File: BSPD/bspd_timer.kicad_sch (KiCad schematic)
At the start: 6 parts, among them U20 HEF4093B, U21 LM555N

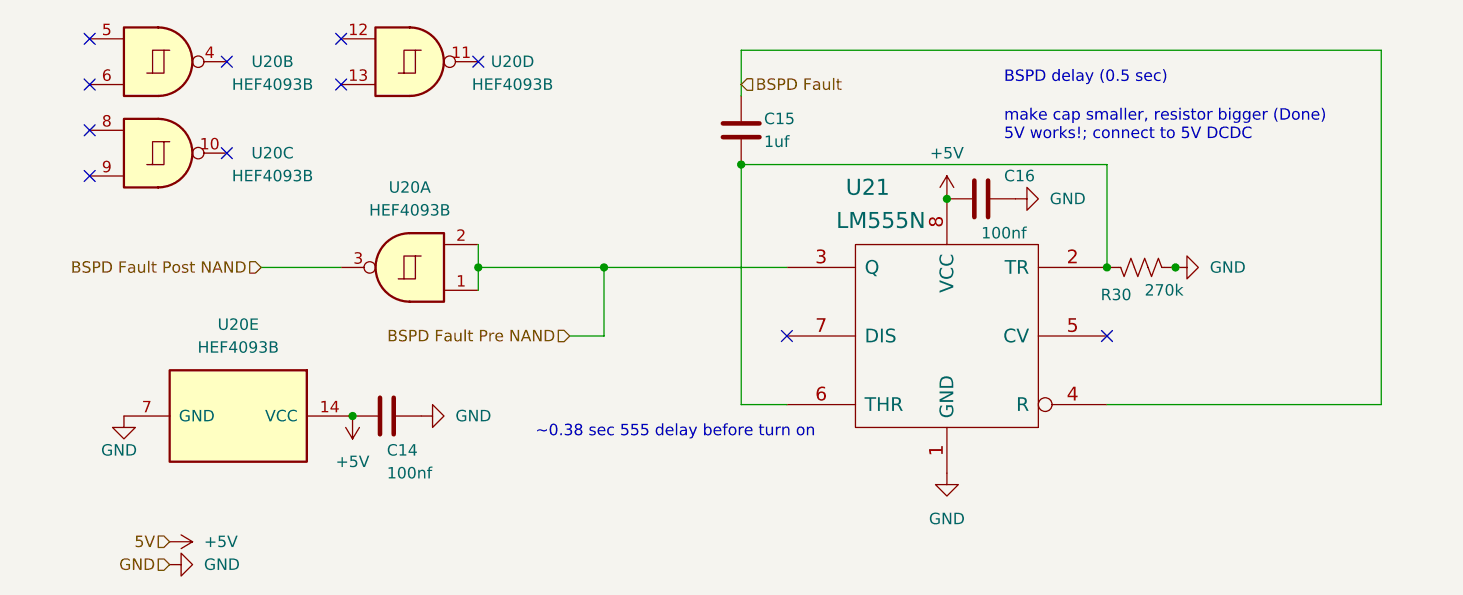
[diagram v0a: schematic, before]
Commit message: Overhaul of BPSD to V3.0
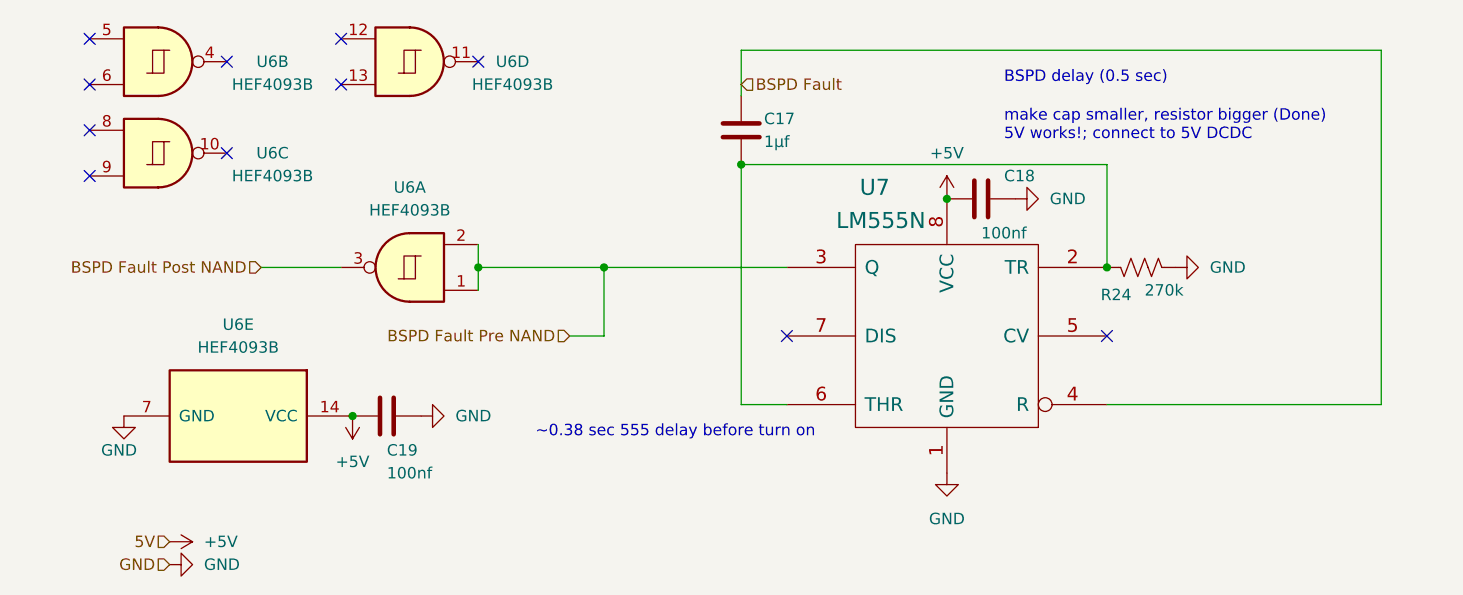
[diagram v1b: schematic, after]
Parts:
- C17: renamed from C15; value 1uf -> 1μf
- renumbered C16 to C18, C14 to C19, R30 to R24, U20 to U6, U21 to U7
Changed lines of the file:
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@@
-	)
-	(junction
-		(at 139.7 44.45)
-		(diameter 0)
-		(color 0 0 0 0)
 	)
 	(junction
@@
 		(pts
 			(xy 46.99 44.45) (xy 38.1 44.45)
-		)
-		(stroke
-			(width 0)
-			(type default)
-		)
-	)
-	(wire
-		(pts
-			(xy 139.7 44.45) (xy 139.7 44.323)
 		)
 		(stroke
@@
 		(on_board yes)
 		(dnp no)
-		(property "Reference" "C14"
+		(property "Reference" "C19"
 			(at 52.07 64.77 90)
 			(effects
@@
 			(project "BSPD"
 				(path "/9b958334-fa88-4811-8197-71444a07b1b5/5dba9582-9d62-469b-9332-e1b404bf542e"
-					(reference "C14")
+					(reference "C19")
 					(unit 1)
 				)
@@
 		(on_board yes)
 		(dnp no)
-		(property "Reference" "R30"
+		(property "Reference" "R24"
 			(at 133.096 47.498 90)
 			(effects
@@
 			(project "BSPD"
 				(path "/9b958334-fa88-4811-8197-71444a07b1b5/5dba9582-9d62-469b-9332-e1b404bf542e"
-					(reference "R30")
+					(reference "R24")
 					(unit 1)
 				)
@@
 		(dnp no)
 		(fields_autoplaced yes)
-		(property "Reference" "U20"
+		(property "Reference" "U6"
 			(at 35.56 50.8 90)
 			(effects
@@
 			(project "BSPD"
 				(path "/9b958334-fa88-4811-8197-71444a07b1b5/5dba9582-9d62-469b-9332-e1b404bf542e"
-					(reference "U20")
+					(reference "U6")
 					(unit 5)
 				)
@@
 		(on_board yes)
 		(dnp no)
-		(property "Reference" "U20"
+		(property "Reference" "U6"
 			(at 66.04 21.59 0)
 			(effects
@@
 			(project "BSPD"
 				(path "/9b958334-fa88-4811-8197-71444a07b1b5/5dba9582-9d62-469b-9332-e1b404bf542e"
-					(reference "U20")
+					(reference "U6")
 					(unit 4)
 				)
@@
 		(dnp no)
 		(fields_autoplaced yes)
-		(property "Reference" "U20"
+		(property "Reference" "U6"
 			(at 54.6183 35.56 0)
 			(effects
@@
 			(project "BSPD"
 				(path "/9b958334-fa88-4811-8197-71444a07b1b5/5dba9582-9d62-469b-9332-e1b404bf542e"
-					(reference "U20")
+					(reference "U6")
 					(unit 1)
 				)
@@
 		(on_board yes)
 		(dnp no)
-		(property "Reference" "C16"
+		(property "Reference" "C18"
 			(at 120.65 34.29 90)
 			(effects
@@
 			(project "BSPD"
 				(path "/9b958334-fa88-4811-8197-71444a07b1b5/5dba9582-9d62-469b-9332-e1b404bf542e"
-					(reference "C16")
+					(reference "C18")
 					(unit 1)
 				)
@@
 		(on_board yes)
 		(dnp no)
-		(property "Reference" "U21"
+		(property "Reference" "U7"
 			(at 107.95 35.56 0)
 			(effects
@@
 			(project "BSPD"
 				(path "/9b958334-fa88-4811-8197-71444a07b1b5/5dba9582-9d62-469b-9332-e1b404bf542e"
-					(reference "U21")
+					(reference "U7")
 					(unit 1)
 				)
@@
 		(on_board yes)
 		(dnp no)
-		(property "Reference" "U20"
+		(property "Reference" "U6"
 			(at 39.37 31.75 0)
 			(effects
@@
 			(project "BSPD"
 				(path "/9b958334-fa88-4811-8197-71444a07b1b5/5dba9582-9d62-469b-9332-e1b404bf542e"
-					(reference "U20")
+					(reference "U6")
 					(unit 3)
 				)
@@
 		(on_board yes)
 		(dnp no)
-		(property "Reference" "U20"
+		(property "Reference" "U6"
 			(at 39.37 21.59 0)
 			(effects
@@
 			(project "BSPD"
 				(path "/9b958334-fa88-4811-8197-71444a07b1b5/5dba9582-9d62-469b-9332-e1b404bf542e"
-					(reference "U20")
+					(reference "U6")
 					(unit 2)
 				)
@@
 		(on_board yes)
 		(dnp no)
-		(property "Reference" "C15"
+		(property "Reference" "C17"
 			(at 93.98 27.94 0)
 			(effects
@@
 			)
 		)
-		(property "Value" "1uf"
+		(property "Value" "1μf"
 			(at 93.98 30.48 0)
 			(effects
@@
 			(project "BSPD"
 				(path "/9b958334-fa88-4811-8197-71444a07b1b5/5dba9582-9d62-469b-9332-e1b404bf542e"
-					(reference "C15")
+					(reference "C17")
 					(unit 1)
 				)
